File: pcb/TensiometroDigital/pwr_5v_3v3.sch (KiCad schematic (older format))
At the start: 9 parts

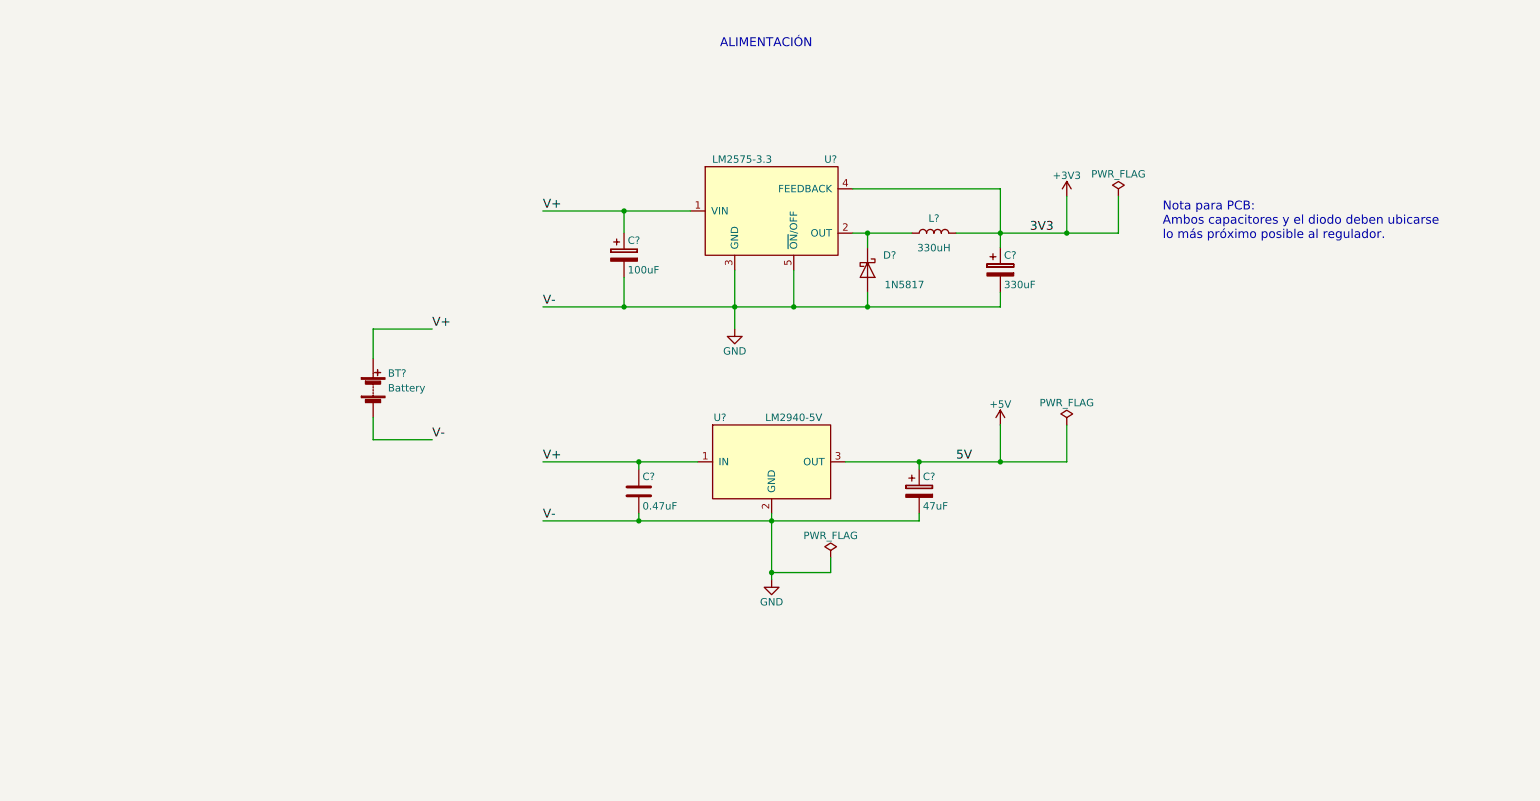
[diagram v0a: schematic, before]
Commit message: Finalizado: SCH, PCB, GABINETE, DRAWINGS. FALTA: GERBERS, BOM e Informe
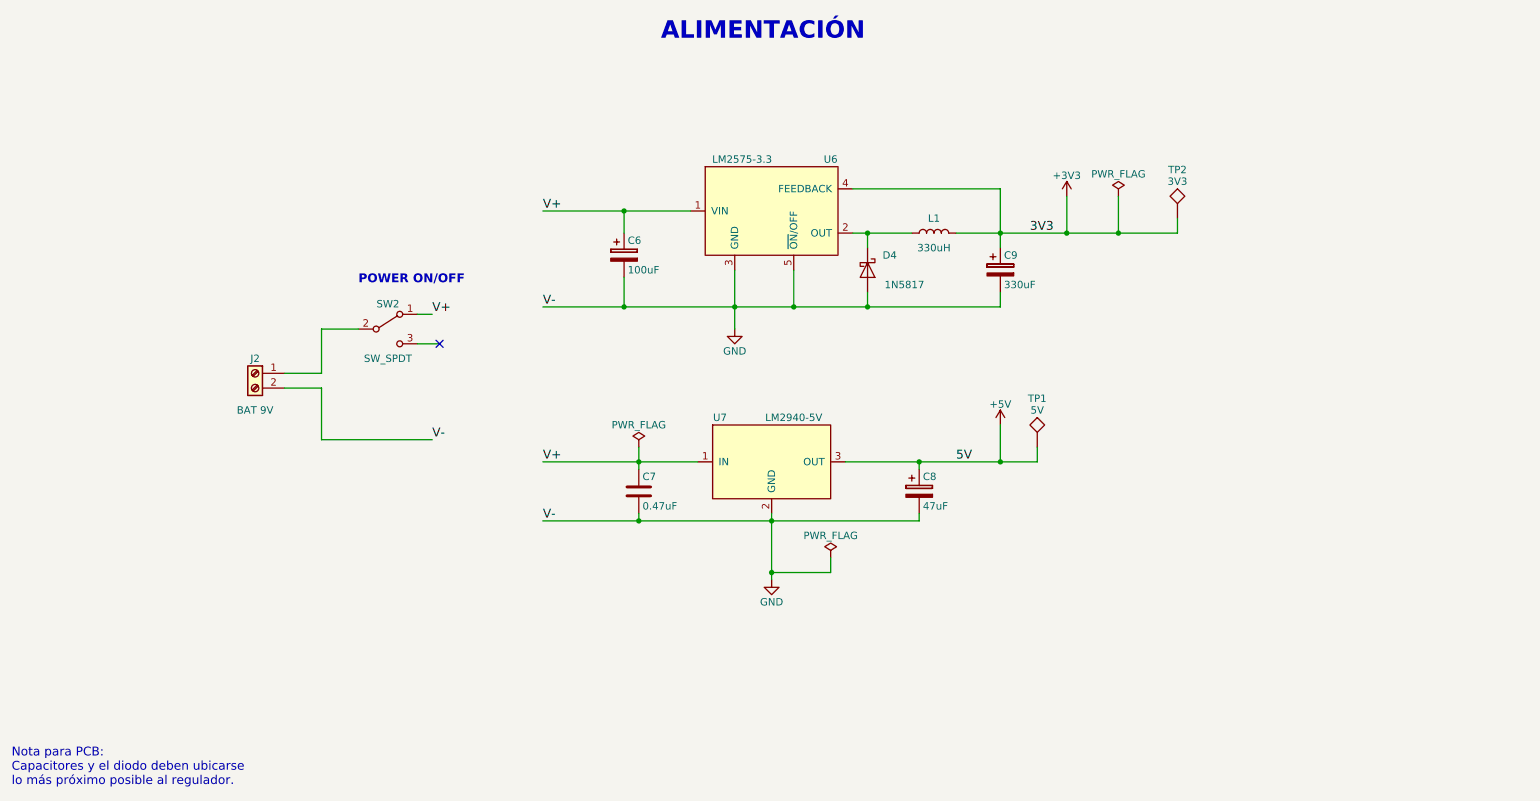
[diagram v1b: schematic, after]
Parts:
- removed BT?: Battery, symbol Battery
- added J2: BAT 9V, footprints:TerminalBlock_bornier-2_P5.08mm, symbol Screw_Terminal_01x02
- added SW2: SW_SPDT, footprints:E_SWITCH_100SP5T4B4VS2QE, symbol SW_SPDT
- added TP1: 5V, footprints:TestPoint_THTPad_D1.5mm_Drill0.7mm, symbol TEST
- added TP2: 3V3, footprints:TestPoint_THTPad_D1.5mm_Drill0.7mm, symbol TEST
- C6: renamed from C?; footprint (none) -> Capacitors_SMD:CP_Elec_6.3x5.8; manf# (none) -> UCQ1A101MCL1GS
- C7: renamed from C?; footprint (none) -> Capacitors_SMD:CP_Elec_4x5.7; manf# (none) -> 865250640004
- C8: renamed from C?; footprint (none) -> Capacitors_SMD:CP_Elec_6.3x4.5; manf# (none) -> UCQ1C470MCL1GB
- C9: renamed from C?; footprint (none) -> Capacitors_SMD:CP_Elec_6.3x7.7; manf# (none) -> 865090145008
- D4: renamed from D?; footprint (none) -> Diodes_THT:D_DO-41_SOD81_P10.16mm_Horizontal; manf# (none) -> 1N5817
- L1: renamed from L?; footprint (none) -> footprints:RFC1010; manf# (none) -> RFC1010B-334KE
- U6: renamed from U?; footprint (none) -> TO_SOT_Packages_SMD:TO-263-5_TabPin3; manf# (none) -> LM2575-3.3WU
- U7: renamed from U?; footprint (none) -> TO_SOT_Packages_SMD:SOT-223-3_TabPin2; manf# (none) -> LM2940IMP-5.0/NOPB
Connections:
- net +3V3: now also TP2.1
- net +5V: now also TP1.1
- net GND: now also J2.2 (Pin_2)
- net V+: now also SW2.1 (A)
- new net: J2.1 (Pin_1), SW2.2 (B)
- no-connect marks 0 -> 1
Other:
- note added: "Nota para PCB: \nCapacitores y el diodo deben ubicarse \nlo más próximo posible al regulador."
- note added: "POWER ON/OFF"
- note removed: "Nota para PCB: \nAmbos capacitores y el diodo deben ubicarse \nlo más próximo posible al regulador."
